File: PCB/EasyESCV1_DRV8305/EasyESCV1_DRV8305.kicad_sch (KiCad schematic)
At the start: 0 parts

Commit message: Finished REV1 Schematic Awaiting Review
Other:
- company: (none) -> Buckley Boards 
- title: (none) -> Easy ESC
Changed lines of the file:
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@@
 	(generator_version "8.0")
 	(paper "A4")
+	(title_block
+		(title "Easy ESC")
+		(date "2024-08-06")
+		(rev "1.0")
+		(company "Buckley Boards ")
+	)
 	(sheet
 		(at 115.57 71.12)
@@
 			(project "EasyESCV1_DRV8305"
 				(path "/6c304649-7c80-4a4c-b925-07b9210ad53d"
-					(page "3")
+					(page "1")
 				)
 			)
@@
 			(project "EasyESCV1_DRV8305"
 				(path "/6c304649-7c80-4a4c-b925-07b9210ad53d"
-					(page "4")
+					(page "3")
 				)
 			)
@@
 			(project "EasyESCV1_DRV8305"
 				(path "/6c304649-7c80-4a4c-b925-07b9210ad53d"
-					(page "3")
+					(page "2")
 				)
 			)

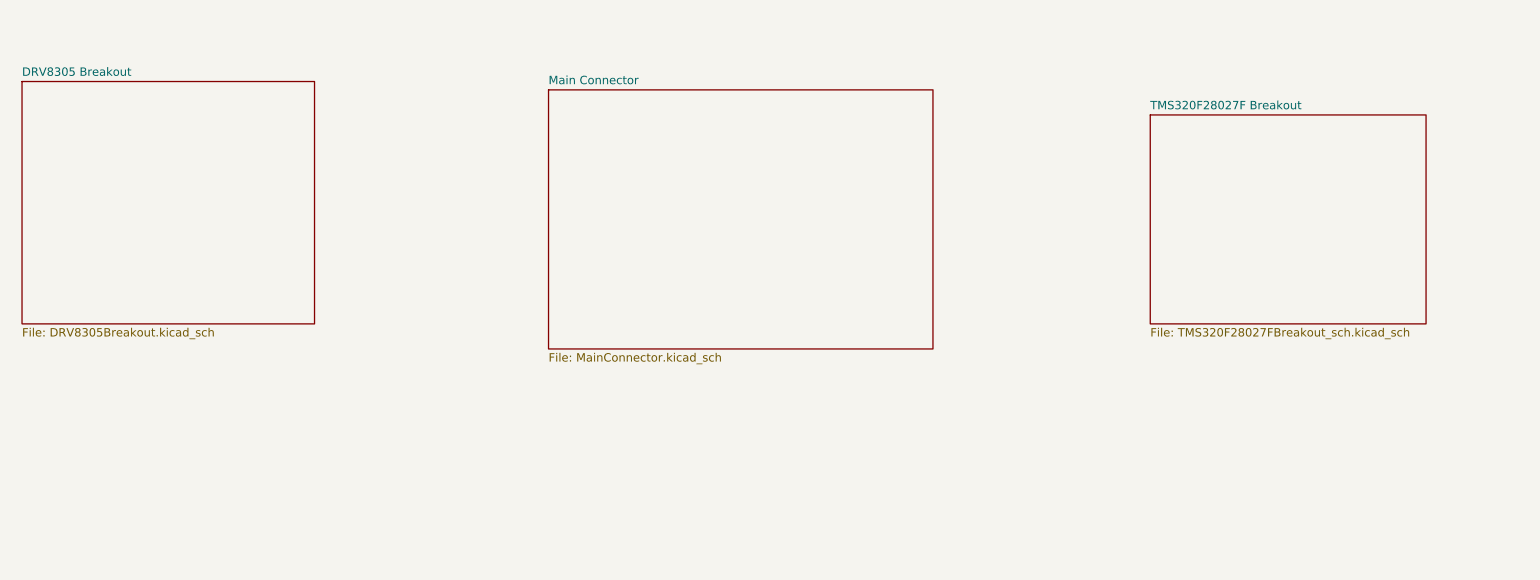
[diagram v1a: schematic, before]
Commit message: Updated Some Errors in Schematic
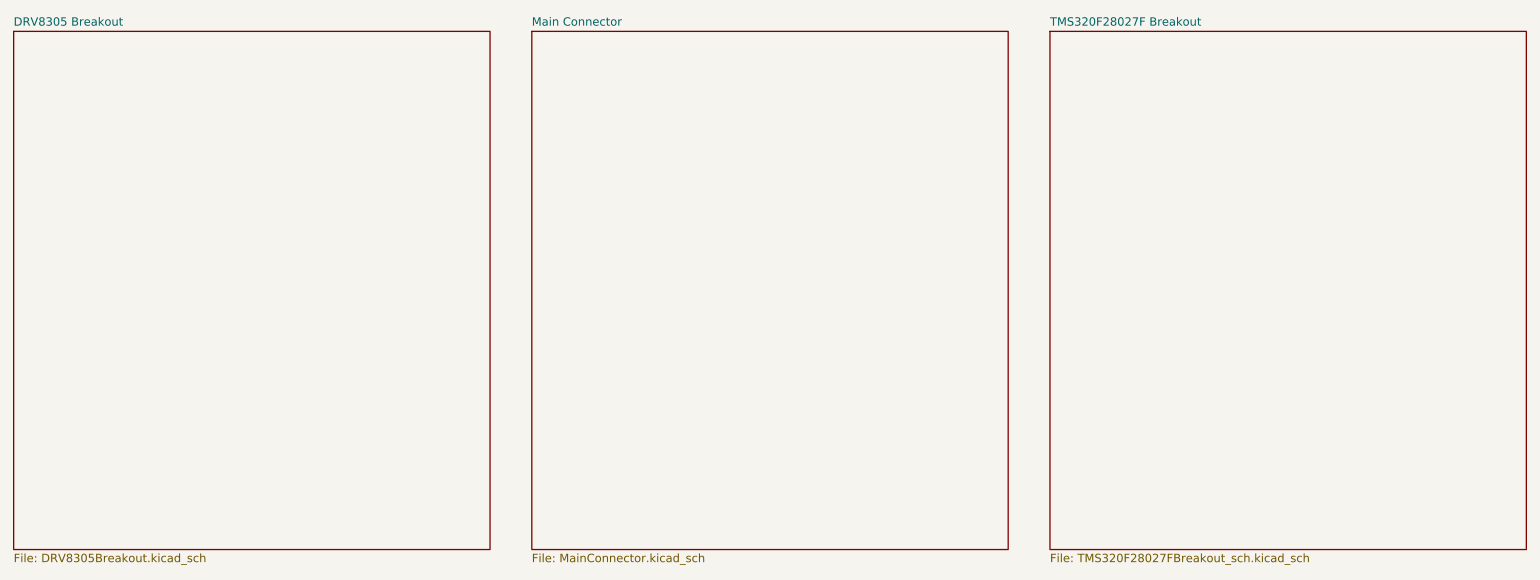
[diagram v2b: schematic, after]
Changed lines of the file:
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@@
 	)
 	(sheet
-		(at 115.57 71.12)
-		(size 58.42 39.37)
+		(at 113.03 62.23)
+		(size 72.39 78.74)
 		(fields_autoplaced yes)
 		(stroke
@@
 		)
 		(property "Sheetname" "Main Connector"
-			(at 115.57 70.4084 0)
+			(at 113.03 61.5184 0)
 			(effects
 				(font
@@
 		)
 		(property "Sheetfile" "MainConnector.kicad_sch"
-			(at 115.57 111.0746 0)
+			(at 113.03 141.5546 0)
 			(effects
 				(font
@@
 	)
 	(sheet
-		(at 207.01 74.93)
-		(size 41.91 31.75)
+		(at 191.77 62.23)
+		(size 72.39 78.74)
 		(fields_autoplaced yes)
 		(stroke
@@
 		)
 		(property "Sheetname" "TMS320F28027F Breakout"
-			(at 207.01 74.2184 0)
+			(at 191.77 61.5184 0)
 			(effects
 				(font
@@
 		)
 		(property "Sheetfile" "TMS320F28027FBreakout_sch.kicad_sch"
-			(at 207.01 107.2646 0)
+			(at 191.77 141.5546 0)
 			(effects
 				(font
@@
 	)
 	(sheet
-		(at 35.56 69.85)
-		(size 44.45 36.83)
+		(at 34.29 62.23)
+		(size 72.39 78.74)
 		(fields_autoplaced yes)
 		(stroke
@@
 		)
 		(property "Sheetname" "DRV8305 Breakout"
-			(at 35.56 69.1384 0)
+			(at 34.29 61.5184 0)
 			(effects
 				(font
@@
 		)
 		(property "Sheetfile" "DRV8305Breakout.kicad_sch"
-			(at 35.56 107.2646 0)
+			(at 34.29 141.5546 0)
 			(effects
 				(font
